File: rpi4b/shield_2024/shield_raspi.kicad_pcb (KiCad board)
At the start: 2 copper layers, 12 parts, among them J1 VL53, J10 LED, J11 LED, J2 LED, J3 LED, J4 Conn_02x20_Odd_Even, J5 Conn_01x04_Pin, J6 Conn_01x04_Pin, J7 VL53, J8 VL53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

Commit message: placement composant
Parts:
- removed J1, J7, J8, J9: VL53, Connector_PinHeader_2.54mm:PinHeader_1x05_P2.54mm_Vertical
- removed J10, J11, J2, J3: LED, Connector_PinHeader_2.54mm:PinHeader_1x02_P2.54mm_Vertical
- removed J5, J6: Conn_01x04_Pin, Connector_PinHeader_2.54mm:PinHeader_1x04_P2.54mm_Vertical
- added BTN_1: BTN_1, Connector_PinHeader_2.54mm:PinHeader_1x02_P2.54mm_Vertical, F.Cu at (74.3, 98.2)
- added BTN_2: BTN_2, Connector_PinHeader_2.54mm:PinHeader_1x02_P2.54mm_Vertical, F.Cu at (74.3, 106.2)
- added H1: MountingHole, MountingHole:MountingHole_3.2mm_M3, F.Cu at (71.3, 74.9)
- added H2: MountingHole, MountingHole:MountingHole_3.2mm_M3, F.Cu at (129.3, 74.9)
- added H3: MountingHole, MountingHole:MountingHole_3.2mm_M3, F.Cu at (129.3, 123.9)
- added H4: MountingHole, MountingHole:MountingHole_3.2mm_M3, F.Cu at (71.3, 123.9)
- added LED_1: LED_1, Connector_PinHeader_2.54mm:PinHeader_1x02_P2.54mm_Vertical, F.Cu at (128.9, 106.2)
- added LED_2: LED_2, Connector_PinHeader_2.54mm:PinHeader_1x02_P2.54mm_Vertical, F.Cu at (128.9, 98.2)
- added R1: R, Resistor_SMD:R_0603_1608Metric, F.Cu at (127.2, 103.2)
- added R2: R, Resistor_SMD:R_0603_1608Metric, F.Cu at (127.2, 101.2)
- added UART_1: Conn_01x04_Pin, Connector_PinHeader_2.54mm:PinHeader_1x04_P2.54mm_Vertical, F.Cu at (100.3, 119.8)
- added UART_2: Conn_01x04_Pin, Connector_PinHeader_2.54mm:PinHeader_1x04_P2.54mm_Vertical, F.Cu at (100.3, 92.2)
- added VL53_1: VL53, Connector_PinHeader_2.54mm:PinHeader_1x05_P2.54mm_Vertical, F.Cu at (120.3, 92.2)
- added VL53_2: VL53, Connector_PinHeader_2.54mm:PinHeader_1x05_P2.54mm_Vertical, F.Cu at (80.3, 92.2)
- added VL53_3: VL53, Connector_PinHeader_2.54mm:PinHeader_1x05_P2.54mm_Vertical, F.Cu at (120.3, 122.4)
- added VL53_4: VL53, Connector_PinHeader_2.54mm:PinHeader_1x05_P2.54mm_Vertical, F.Cu at (80.3, 122.4)
- moved U1 85.0 mm to (225.8, 80.1)
- moved J4 33.6 mm to (76.2, 76.2)
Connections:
- J4 pad 18: GPIO24 -> BTN_1
- J4 pad 22: GPIO25 -> BTN_2
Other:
- board outline added: 66 x 57 mm
- board text added: "PWM0"
- board text added: "PWM1"

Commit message: routage préliminaire
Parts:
- removed UART_1, UART_2: Conn_01x04_Pin, Connector_PinHeader_2.54mm:PinHeader_1x04_P2.54mm_Vertical
- added UART_3: Conn_01x04_Pin, Connector_PinHeader_2.54mm:PinHeader_1x04_P2.54mm_Vertical, F.Cu at (89.4, 104.6)
- added UART_4: Conn_01x04_Pin, Connector_PinHeader_2.54mm:PinHeader_1x04_P2.54mm_Vertical, F.Cu at (89.4, 84.6)
- R1, R2: moved to B.Cu
- moved H2 13.3 mm to (118.4, 67.3)
- moved H3 13.3 mm to (118.4, 116.3)
- moved LED_1 13.3 mm to (117.9, 98.6)
- moved LED_2 13.3 mm to (117.9, 90.6)
- moved BTN_1 13.3 mm to (63.4, 90.6)
- moved BTN_2 13.3 mm to (63.4, 98.6)
- moved H1 13.3 mm to (60.4, 67.3)
- moved H4 13.3 mm to (60.4, 116.3)
- moved J4 13.3 mm to (65.3, 68.6)
- moved R1 13.3 mm to (116.2, 95.6)
- moved R2 13.3 mm to (116.2, 93.6)
- moved VL53_1 13.3 mm to (109.4, 84.6)
- moved VL53_2 13.3 mm to (69.4, 84.6)
- moved VL53_3 13.3 mm to (109.4, 114.7)
- moved VL53_4 13.3 mm to (69.4, 114.7)
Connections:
- J4 pad 10: GPIO15_RXD0_RXD1 -> unconnected-(J4-Pin_10-Pad10)
- J4 pad 11: GPIO17 -> unconnected-(J4-Pin_11-Pad11)
- J4 pad 13: GPIO27 -> unconnected-(J4-Pin_13-Pad13)
- J4 pad 15: GPIO22_SDA6 -> unconnected-(J4-Pin_15-Pad15)
- J4 pad 16: GPIO23_SCL6 -> unconnected-(J4-Pin_16-Pad16)
- J4 pad 19: GPIO10_SDA5 -> unconnected-(J4-Pin_19-Pad19)
- J4 pad 23: GPIO11_SCL5 -> unconnected-(J4-Pin_23-Pad23)
- J4 pad 26: GPIO7_SCL4 -> unconnected-(J4-Pin_26-Pad26)
- J4 pad 31: GPIO6_SDA4 -> unconnected-(J4-Pin_31-Pad31)
- J4 pad 33: VL53_1 -> VL53_3
- J4 pad 35: VL53_3 -> VL53_1
- J4 pad 36: GPIO16 -> unconnected-(J4-Pin_36-Pad36)
- J4 pad 37: GPIO26 -> unconnected-(J4-Pin_37-Pad37)
- J4 pad 8: GPIO14_TXD0_TXD1 -> unconnected-(J4-Pin_8-Pad8)
- LED_1 pad 1: LED_1 -> LED_2
- LED_2 pad 1: LED_2 -> LED_1
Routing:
- net +3.3V: track 0.00 -> 169.8 mm, vias 0 -> 1
- net SDA: track 0.00 -> 122.7 mm
- net SCL: track 0.00 -> 108.7 mm, vias 0 -> 1
- net VL53_4: track 0.00 -> 77.4 mm
- net +5V: track 0.00 -> 59.9 mm, vias 0 -> 2
- net BTN_2: track 0.00 -> 49.5 mm, vias 0 -> 1
- net RXD3: track 0.00 -> 48.4 mm
- net TXD3: track 0.00 -> 48.0 mm
- net BTN_1: track 0.00 -> 44.9 mm, vias 0 -> 2
- net LED_2: track 0.00 -> 37.5 mm
- net VL53_3: track 0.00 -> 37.4 mm
- net LED_1: track 0.00 -> 29.4 mm
- net GND: track 0.00 -> 15.2 mm
- net TXD4: track 0.00 -> 15.0 mm
- net VL53_2: track 0.00 -> 14.5 mm
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- added copper zone on B.Cu, net GND
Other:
- outline, holes or cut-outs redrawn
- board text added: "+3.3V"
- board text added: "+5V"
- board text added: "GND"
- board text added: "OFF"
- board text added: "RX3"
- board text added: "RX4"
- board text added: "SCL"
- board text added: "SDA"
- board text added: "TX3"
- board text added: "TX4"

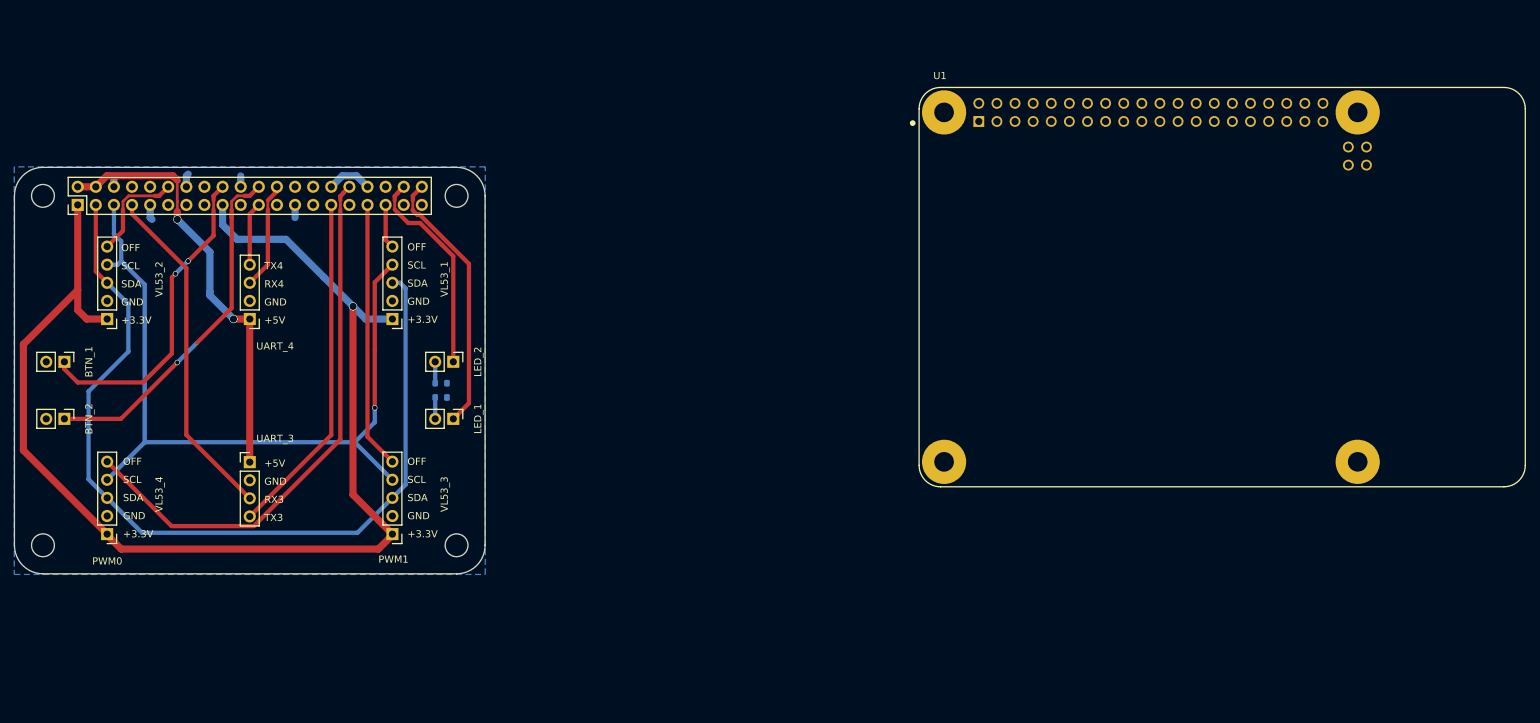
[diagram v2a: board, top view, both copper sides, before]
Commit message: DRC okay, ignore Warnings on H1 & H2 , ready to go
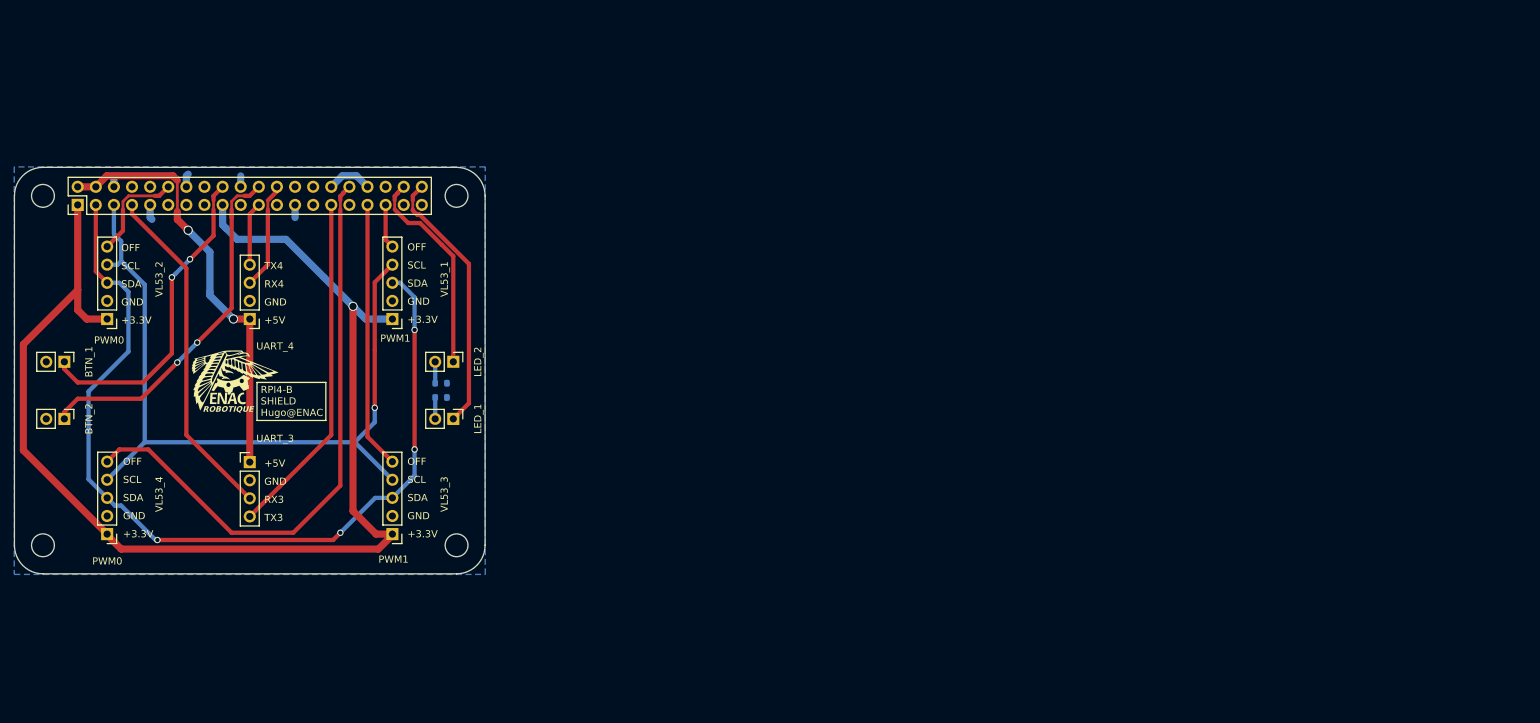
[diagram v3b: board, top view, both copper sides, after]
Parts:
- removed U1: RASPBERRY_PI_4B_4GB, ENAC_robotique:MODULE_RASPBERRY_PI_4B_4GB
- added G***: LOGO, ENAC_robotique:logo_enac_mini, F.Cu at (86.4, 93.0)
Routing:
- net VL53_4: track 77.4 -> 83.4 mm
- net SDA: track 122.7 -> 125.6 mm, vias 0 -> 4
- net +3.3V: track 169.8 -> 171.2 mm
- net BTN_2: track 49.5 -> 50.1 mm, vias 1 -> 2
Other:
- board text added: "RPI4-B SHIELD Hugo@ENAC"

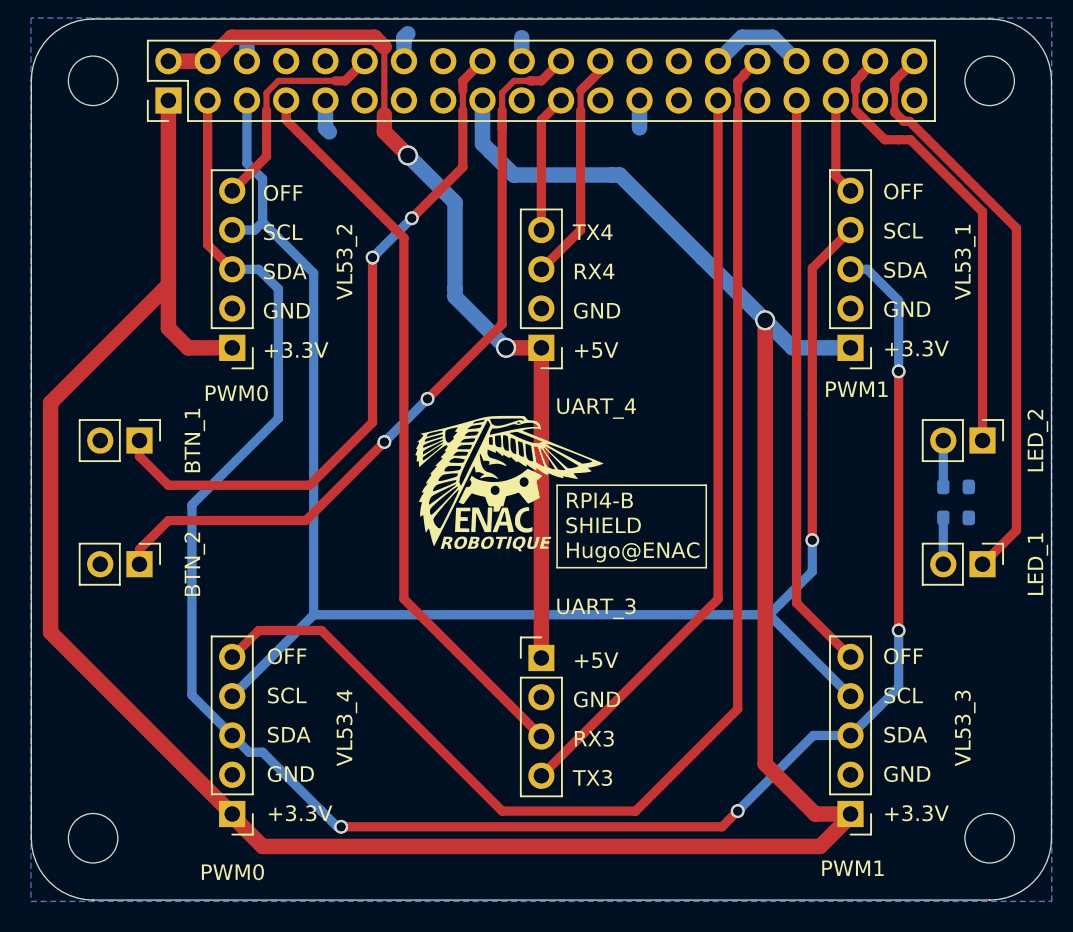
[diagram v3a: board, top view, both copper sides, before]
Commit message: trou ventilateur + molex
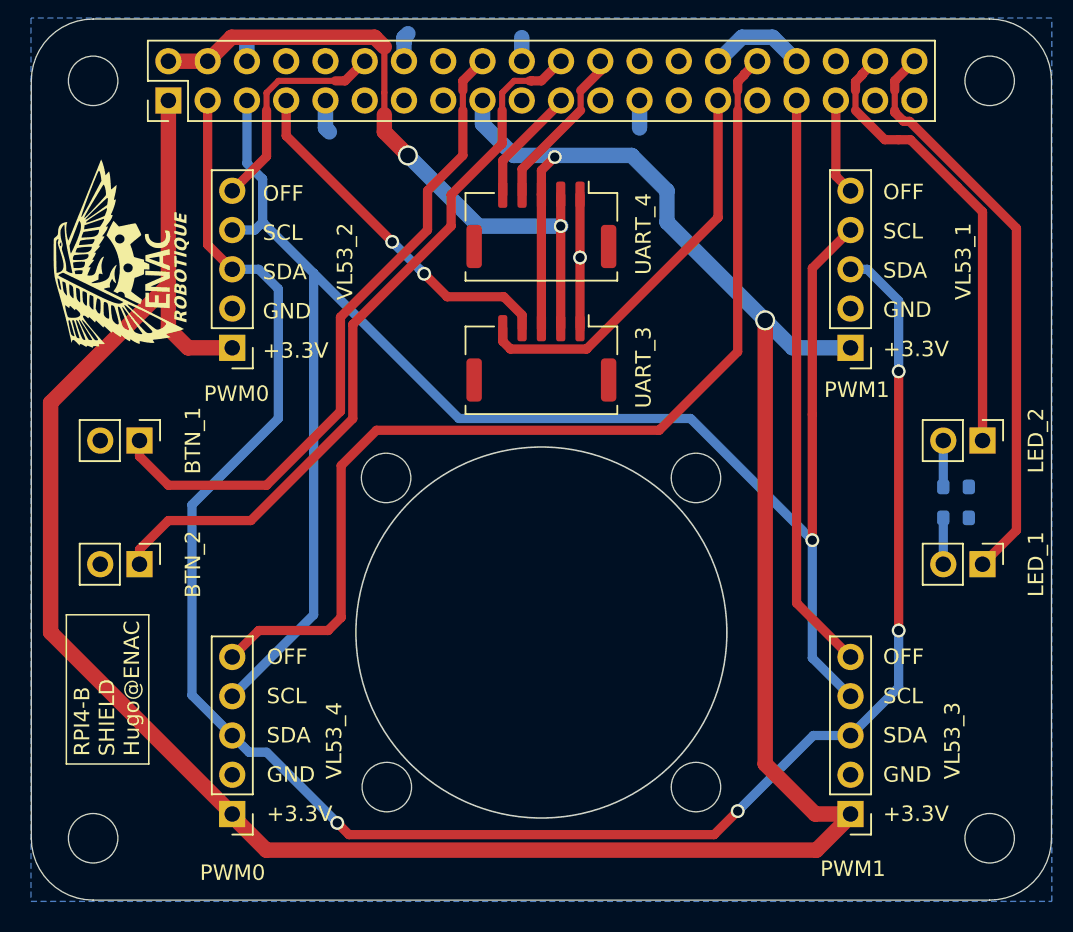
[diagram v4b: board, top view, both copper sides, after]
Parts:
- added H5: MountingHole, MountingHole:MountingHole_3.2mm_M3, F.Cu at (79.4, 93.0)
- added H6: MountingHole, MountingHole:MountingHole_3.2mm_M3, F.Cu at (99.4, 93.0)
- added H7: MountingHole, MountingHole:MountingHole_3.2mm_M3, F.Cu at (79.4, 113.0)
- added H8: MountingHole, MountingHole:MountingHole_3.2mm_M3, F.Cu at (99.4, 113.0)
- UART_3, UART_4: value Conn_01x04_Pin -> Conn_01x05_Pin; footprint Connector_PinHeader_2.54mm:PinHeader_1x04_P2.54mm_Vertical -> Connector_Molex:Molex_CLIK-Mate_502382-0570_1x05-1MP_P1.25mm_Vertical
- moved G*** 28.0 mm to (61.8, 79.5), turned to 90 degrees
- moved UART_3 19.4 mm to (89.4, 85.3), turned to 180 degrees
- moved UART_4 7.96 mm to (89.4, 76.6)
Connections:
- UART_3 pad 1: +5V -> GND
- UART_3 pad 2: GND -> +5V
- UART_3 pad 3: TXD3 -> +3.3V
- UART_3 pad 4: RXD3 -> TXD3
- UART_4 pad 1: +5V -> GND
- UART_4 pad 2: GND -> +5V
- UART_4 pad 3: TXD4 -> +3.3V
- UART_4 pad 4: RXD4 -> TXD4
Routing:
- net TXD3: track 48.0 -> 23.2 mm, vias 0 -> 2
- net RXD3: track 48.4 -> 26.1 mm
- net VL53_4: track 83.4 -> 66.0 mm
- net +5V: track 59.9 -> 42.9 mm
- net +3.3V: track 171.2 -> 183.2 mm, vias 1 -> 2
- net GND: track 15.2 -> 23.8 mm, vias 0 -> 1
- net SCL: track 108.7 -> 116.3 mm
- net TXD4: track 15.0 -> 10.7 mm
- net BTN_2: track 50.1 -> 48.0 mm, vias 2 -> 0
- net BTN_1: track 44.9 -> 43.2 mm, vias 2 -> 0
- net RXD4: track 8.91 -> 7.66 mm
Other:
- outline, holes or cut-outs redrawn
- board text removed: "+5V"
- board text removed: "RX3"
- board text removed: "RX4"
- board text removed: "TX3"
- board text removed: "TX4"

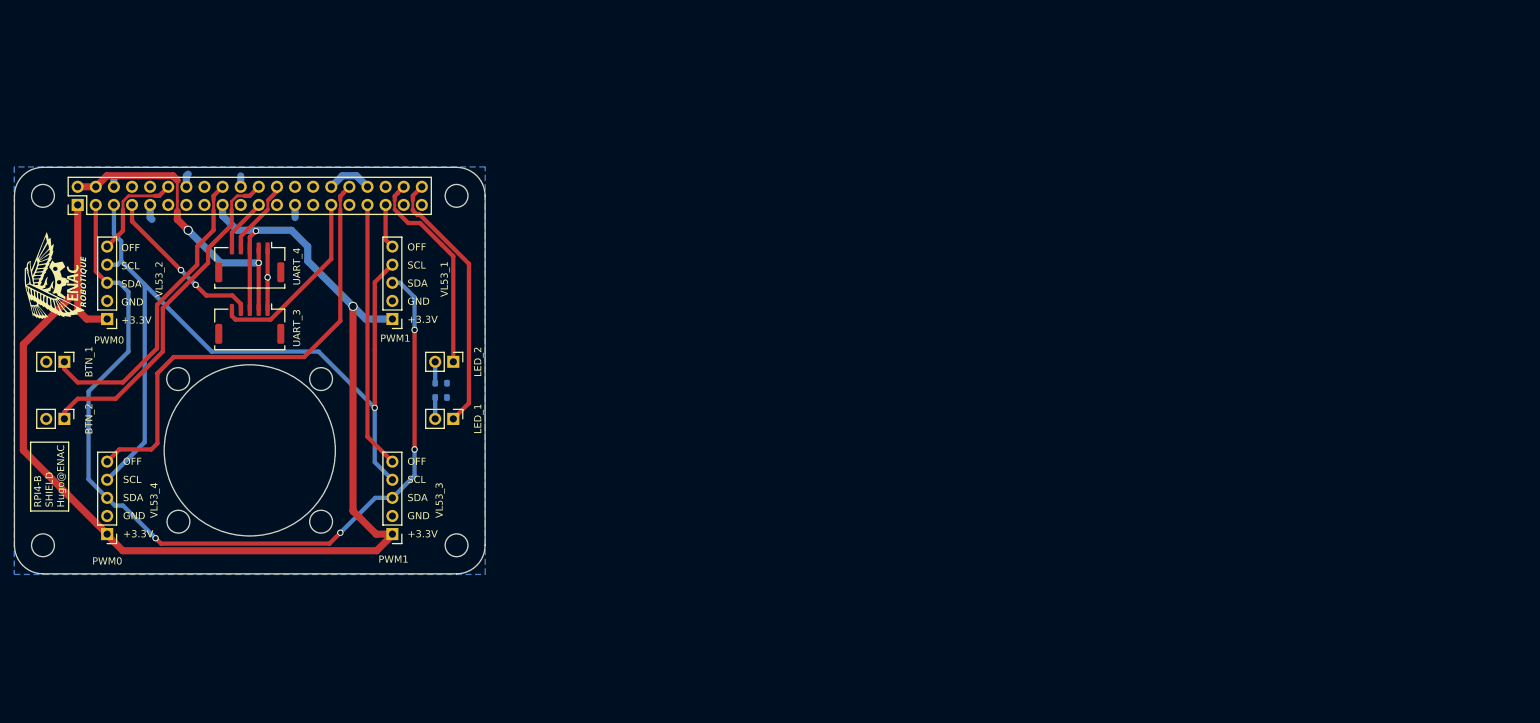
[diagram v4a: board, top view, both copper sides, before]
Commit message: Validation en attente + Add uarts, ventillo
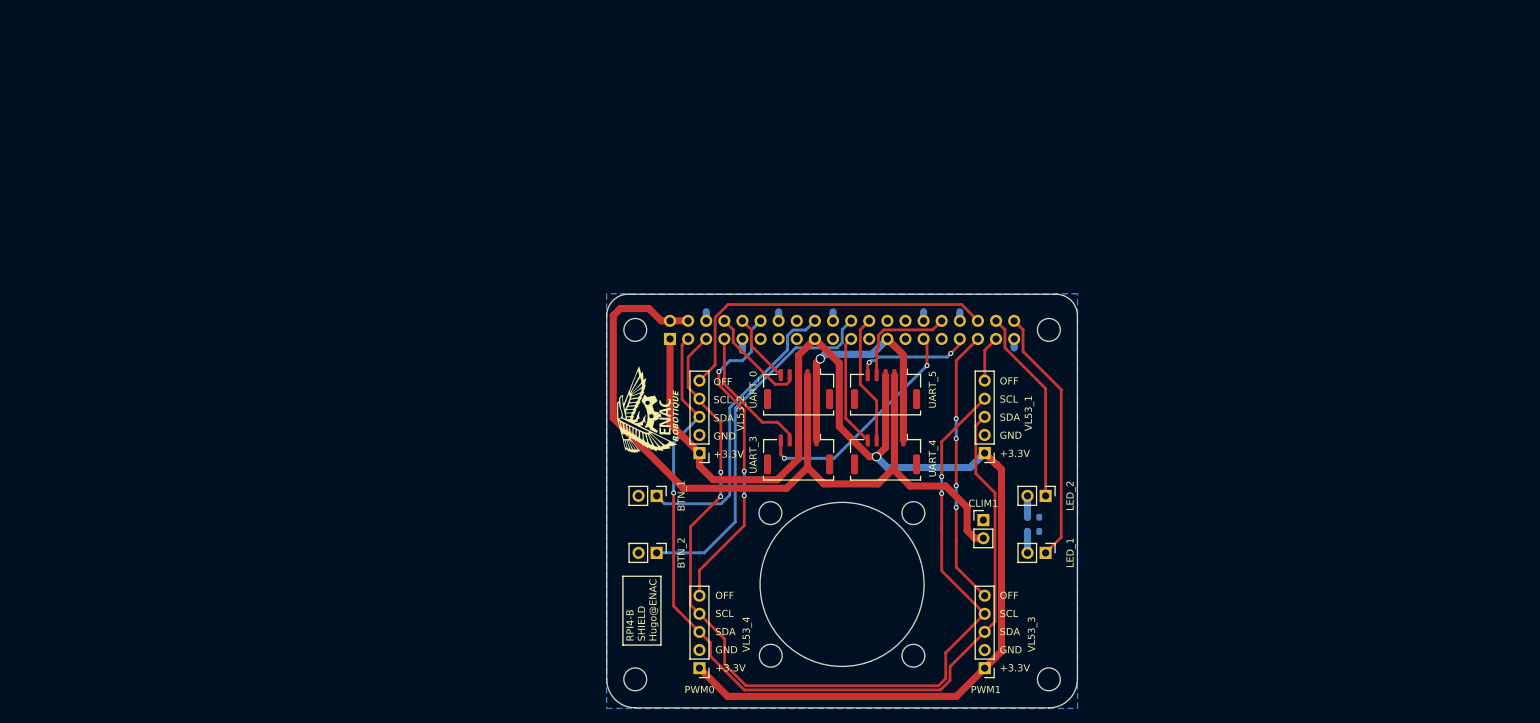
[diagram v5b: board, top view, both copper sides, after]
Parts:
- added CLIM1: CLIM, Connector_PinHeader_2.54mm:PinHeader_1x02_P2.54mm_Vertical, F.Cu at (192.3, 112.8)
- added UART_0: Conn_01x05_Pin, Connector_Molex:Molex_CLIK-Mate_502382-0570_1x05-1MP_P1.25mm_Vertical, F.Cu at (166.4, 94.4)
- added UART_5: Conn_01x05_Pin, Connector_Molex:Molex_CLIK-Mate_502382-0570_1x05-1MP_P1.25mm_Vertical, F.Cu at (178.6, 94.4)
- J4: footprint Connector_PinHeader_2.54mm:PinHeader_2x20_P2.54mm_Vertical -> Connector_PinSocket_2.54mm:PinSocket_2x20_P2.54mm_Vertical; moved to B.Cu
- moved UART_4 93.1 mm to (178.6, 103.5)
- moved G*** 85.2 mm to (144.9, 98.3)
- moved BTN_1 85.2 mm to (146.5, 109.4)
- moved BTN_2 85.2 mm to (146.5, 117.4)
- moved H1 85.2 mm to (143.5, 86.1)
- moved H2 85.2 mm to (201.5, 86.1)
- moved H3 85.2 mm to (201.5, 135.1)
- moved H4 85.2 mm to (143.5, 135.1)
- moved H6 85.2 mm to (182.5, 111.8)
- moved H7 85.2 mm to (162.5, 131.8)
- moved H8 85.2 mm to (182.5, 131.8)
- moved J4 85.2 mm to (148.3, 87.4), turned to -90 degrees
- moved LED_1 85.2 mm to (201.0, 117.4)
- moved LED_2 85.2 mm to (201.0, 109.4)
- moved VL53_1 85.2 mm to (192.5, 103.4)
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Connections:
- J4 pad 10: unconnected-(J4-Pin_10-Pad10) -> RXD0
- J4 pad 12: VL53_2 -> VL53_4
- J4 pad 32: VL53_4 -> TXD5
- J4 pad 33: VL53_3 -> RXD5
- J4 pad 35: VL53_1 -> VL53_3
- J4 pad 36: unconnected-(J4-Pin_36-Pad36) -> VL53_2
- J4 pad 37: unconnected-(J4-Pin_37-Pad37) -> VL53_1
- J4 pad 8: unconnected-(J4-Pin_8-Pad8) -> TXD0
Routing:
- net +5V: track 42.9 -> 117.2 mm, vias 2 -> 0
- net VL53_2: track 14.5 -> 48.3 mm
- net GND: track 23.8 -> 46.6 mm
- net VL53_4: track 66.0 -> 46.1 mm, vias 0 -> 3
- net RXD5: track 0.00 -> 16.4 mm, vias 0 -> 2
- net TXD5: track 0.00 -> 15.4 mm
- net SCL: track 116.3 -> 131.5 mm, vias 1 -> 4
- net TXD0: track 0.00 -> 14.9 mm
- net RXD0: track 0.00 -> 9.85 mm
- net RXD4: track 7.66 -> 15.8 mm
- net TXD4: track 10.7 -> 18.2 mm
- net RXD3: track 26.1 -> 32.0 mm, vias 0 -> 2
- net +3.3V: track 183.2 -> 177.9 mm, vias 2 -> 1
- net TXD3: track 23.2 -> 19.3 mm, vias 2 -> 0
- net BTN_2: track 48.0 -> 51.1 mm
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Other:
- board size 66 x 57 mm -> 66 x 58 mm
- board text added: "UART RX|TX|+3.3|+5|GND"

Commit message: WIP le ventillo
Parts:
- added U1: IRLML2402, myFootprints:SOT-23, B.Cu at (211.5, 98.6)
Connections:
- CLIM1 pad 2: +5V -> Net-(CLIM1-Pin_2)
- J4 pad 31: unconnected-(J4-Pin_31-Pad31) -> CLIM
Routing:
- net +5V: track 117.2 -> 118.2 mm
